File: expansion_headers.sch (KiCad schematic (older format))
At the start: 14 parts, among them J51 rpi_gpio, J52 Conn_02x20_Odd_Even, J54 Conn_02x08_Odd_Even, J56 BOOT, J57 rpi power

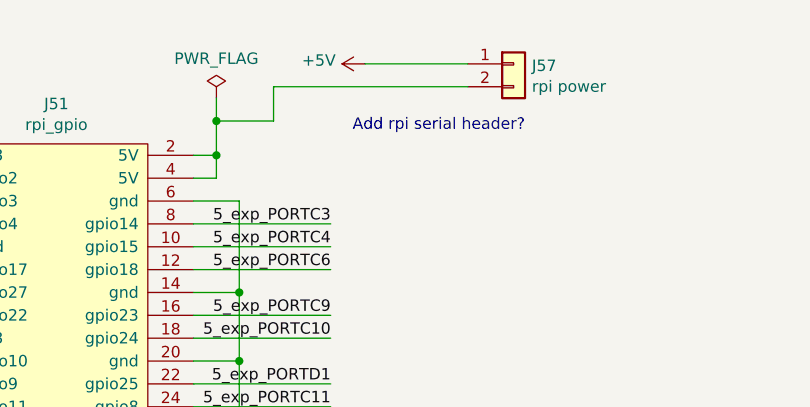
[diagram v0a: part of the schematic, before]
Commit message: Mk.3 fixes and new 68000 expansion board
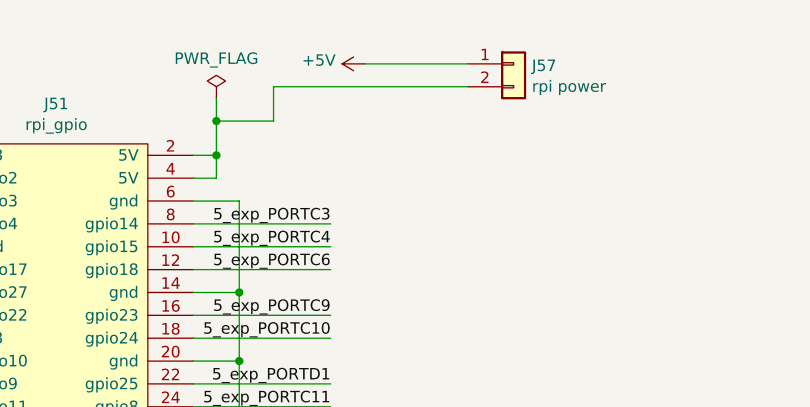
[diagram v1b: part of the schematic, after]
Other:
- note removed: "Add rpi serial header?"
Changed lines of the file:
@@
 Sheet 8 11
 Title "Mk.3 Blitter FPGA development board"
-Date "2021-05-08"
-Rev "3.00"
+Date "2021-08-14"
+Rev "3.03"
 Comp "Dossytronics"
-Comment1 ""
+Comment1 "fixed: clk/sysd0, jtag, u22 footprint"
 Comment2 ""
 Comment3 ""
@@
 Text Label 3500 3900 2    50   ~ 0
 exp_PORTA_DIR
-Text Notes 4300 1000 2    50   ~ 0
-Add rpi serial header?
 Wire Wire Line
 	6800 5200 7800 5200
